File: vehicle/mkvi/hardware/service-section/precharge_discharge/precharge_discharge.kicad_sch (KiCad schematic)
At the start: 13 parts, among them J1 MicroFit_VT_5x1, J2 Automotive_M.2_Edge_Connector, K1 G2RG-2A-X_DC12, K2 3350-4275-126, Q1 SSM3K333R

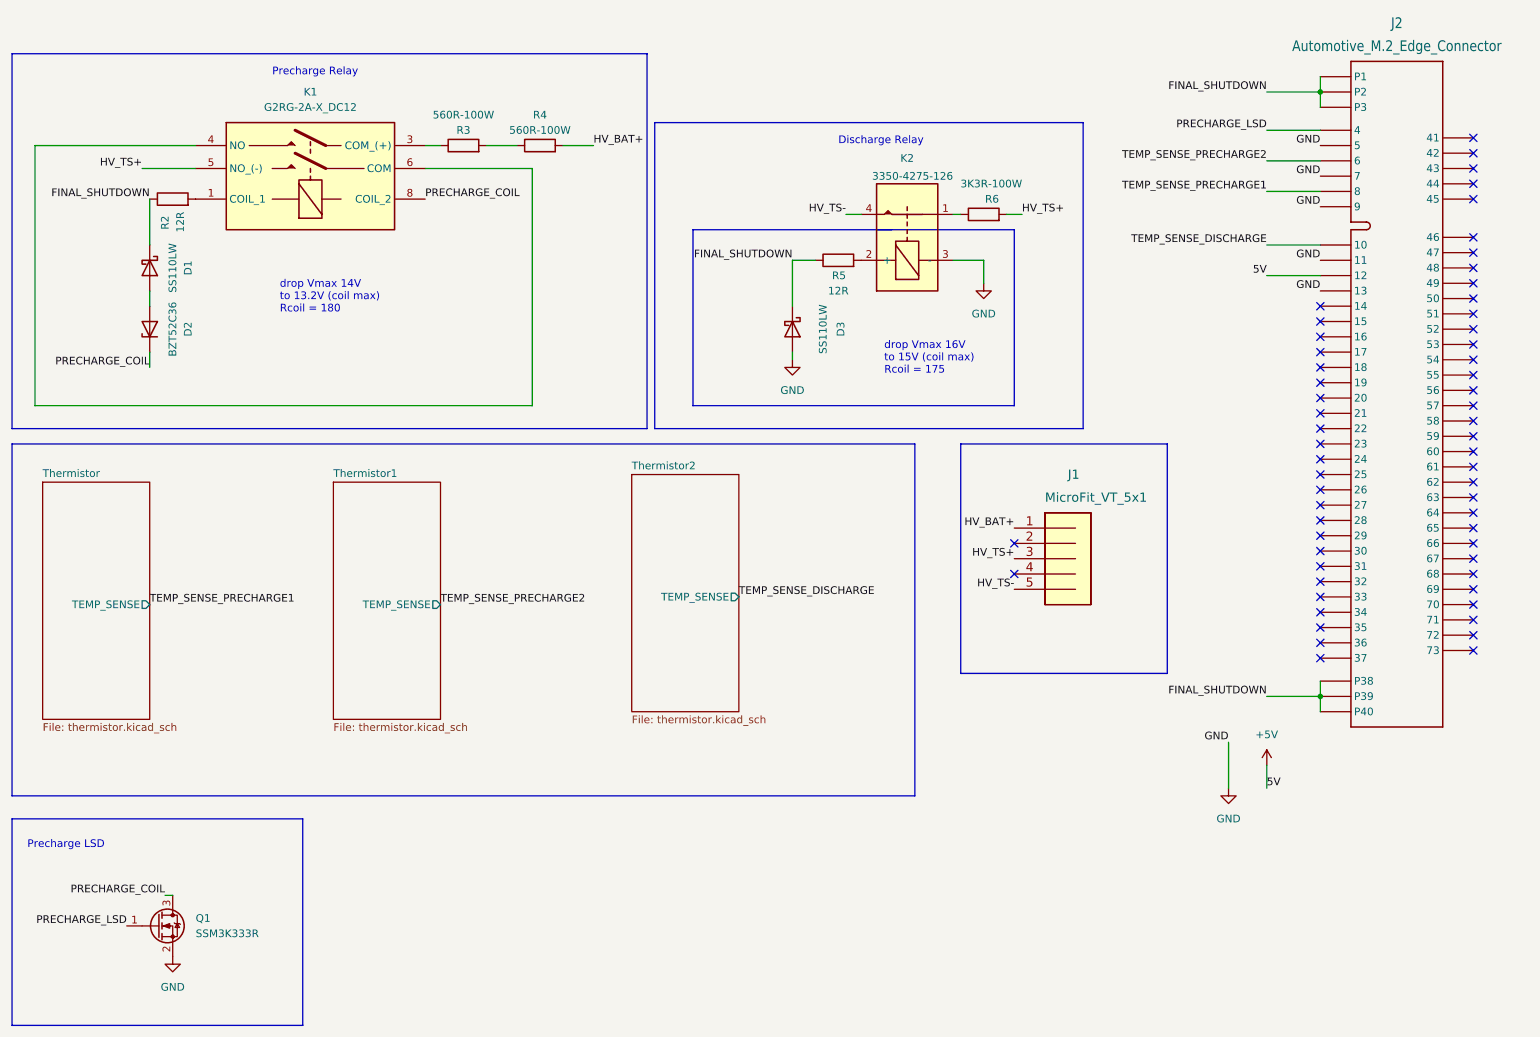
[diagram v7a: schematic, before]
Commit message: Finalize boards for fab (#217)
* add BOM tool to join BOMs

* add custom BOM script for working with custom BOM fields

* add patched QR plugin for better QR codes

* add logo and authors to boards

* update parts library and fix misc issues

* migrate projects to new parts library
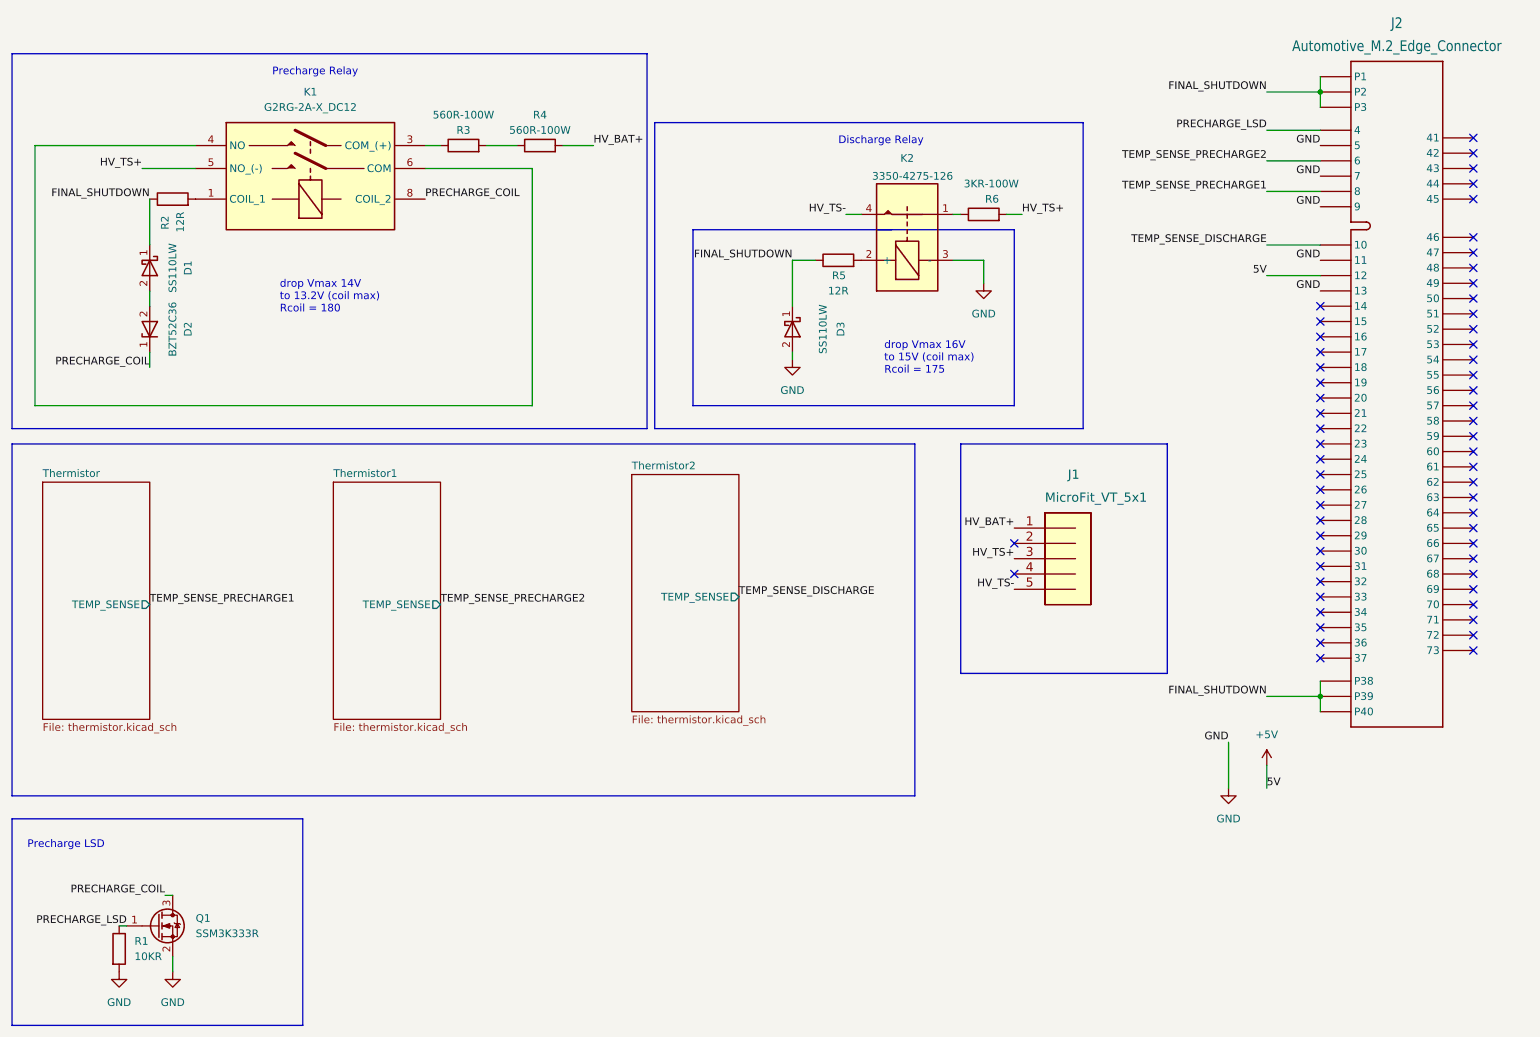
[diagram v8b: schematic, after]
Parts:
- added R1: 10KR, OEM:R_0603, symbol OEM:10KR
- D1, D3: DKPN (none) -> 1801-SS110LWDKR-ND; MFN (none) -> Taiwan Semiconductor Corporation; MPN SS110LWRVGCT-ND -> SS110LW; NewDesigns (none) -> YES; Package (none) -> SOD-123; Stocked (none) -> Tape; Style (none) -> SMD
- D2: DKPN (none) -> BZT52C36-FDICT-ND; MFN (none) -> Diodes; MPN BZT52C36 -> BZT52C36-7-F; NewDesigns (none) -> YES; Package (none) -> SOD123; Stocked (none) -> No; Style (none) -> SMD
- J1: DKPN (none) -> WM1848-ND; MFN (none) -> Molex; MatesWith (none) -> 0436450500; NewDesigns (none) -> YES; Package (none) -> Custom; Stocked (none) -> Loose; Style (none) -> THT
- J2: symbol formula:Automotive_M.2_Edge_Connector -> OEM:Automotive_M.2_Edge_Connector; DKPN (none) -> N/A; MFN (none) -> N/A; MPN (none) -> N/A; NewDesigns (none) -> YES; Package (none) -> N/A; Stocked (none) -> N/A; Style (none) -> Edge Connector; now left out of the parts list
- K1: DKPN (none) -> 39-G2RG-2A-XDC12-ND; MFN (none) -> Omron; MPN (none) -> G2RG-2A-X DC12; NewDesigns (none) -> YES; Package (none) -> Custom; Stocked (none) -> No; Style (none) -> THT
- K2: DKPN (none) -> 1835-1040-ND; MFN (none) -> Comus; NewDesigns (none) -> Yes; Package (none) -> Custom; Stocked (none) -> No; Style (none) -> THT
- Q1: DKPN (none) -> SSM3K333RLFDKR-ND; MFN (none) -> Toshiba; NewDesigns (none) -> YES; Package (none) -> SOT-23; Stocked (none) -> Digi-Reel; Style (none) -> SMD
- R2, R5: footprint footprints:R_0805_OEM -> OEM:R_0603; DKPN (none) -> 311-12.0HRTR-ND; MFN TE -> YAGEO; MPN CPF-A-0805B12RE -> RC0603FR-0712RL; NewDesigns (none) -> YES; Package (none) -> 0603; PurchasingLink https://www.digikey.com/en/products/detail/te-connectivity-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 -> (none); Stocked (none) -> Reel; Style (none) -> SMD
- R3, R4: DKPN (none) -> AP101560RJ-ND; DPN (none) -> AP101560RJ-ND; MFN DK -> Ohmite/Arcol; MPN AP101 560R J -> AP101560RJ; NewDesigns (none) -> YES; Package (none) -> TO247; PurchasingLink https://www.digikey.com/en/products/detail/ohmite/AP101-560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 -> (none); Stocked (none) -> No; Style (none) -> THT
- R6: value 3K3R-100W -> 3KR-100W; symbol OEM:3K3R-100W -> OEM:3KR-100W; DKPN (none) -> AP1013KJ-ND; DPN (none) -> AP1013KJ-ND; MFN (none) -> Ohmite/Arcol; MPN (none) -> AP1013KJ; NewDesigns (none) -> YES; Package (none) -> TO247; Stocked (none) -> No; Style (none) -> THT
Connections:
- net GND: now also R1.2
- net PRECHARGE_LSD: now also R1.1
